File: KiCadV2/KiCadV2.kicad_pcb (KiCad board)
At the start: 2 copper layers, 76.4 x 51.6 mm, 141 parts, among them J1 USB_C_Receptacle_PowerOnly_6P, J3 Screw_Terminal_01x02, J4 Screw_Terminal_01x02, U1 MT3608, U10 NC7SZ157P6X, U11 NC7SZ157P6X, U12 NC7SZ157P6X, U13 NC7SZ157P6X, U14 74LV08AT14-13, U15 HIP4080A, U16 NC7SZ157P6X, U17 MX3502S, U18 MX3502S, U2 74HC595, U22 DMHT10H032LFJ, U26 MX3502S, U3 NC7SZ157P6X, U30 DMHT10H032LFJ, U31 INA240A1D, U32 NC7SZ157P6X, U33 NC7SZ157P6X, U34 NC7SZ157P6X, U35 NC7SZ157P6X, U36 NC7SZ157P6X, U37 NC7SZ157P6X, U38 74LV08AT14-13, U39 HIP4080A, U4 NC7SZ157P6X, U40 MCP6002-xSN, U41 CJ432, U5 MX3502S, U6 NC7SZ157P6X, U7 DAC082S085CISDX/NOPB, U8 NC7SZ157P6X, U9 NC7SZ157P6X

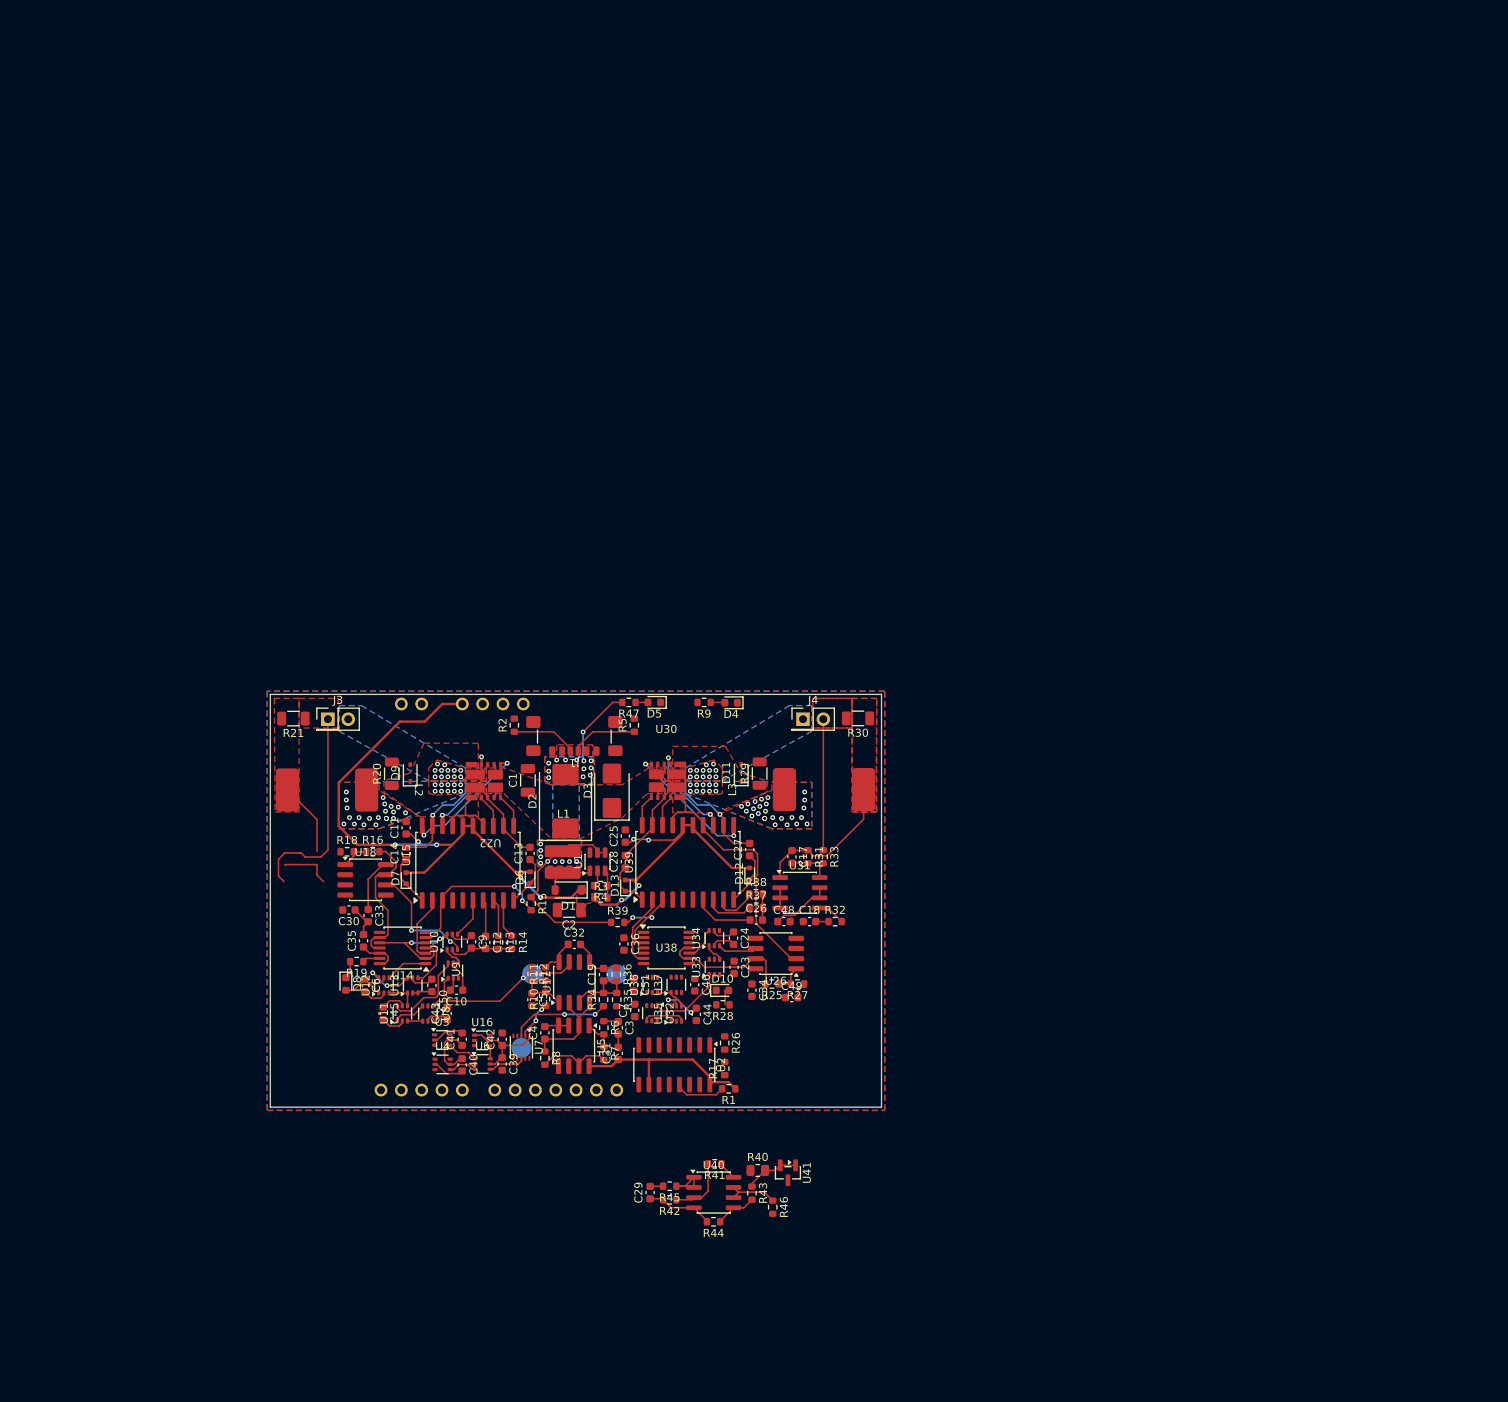
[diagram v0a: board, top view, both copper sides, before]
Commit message: DAC logic
- Internal connections done
- Spacing, shorts, nets, etc verified
- Grouped
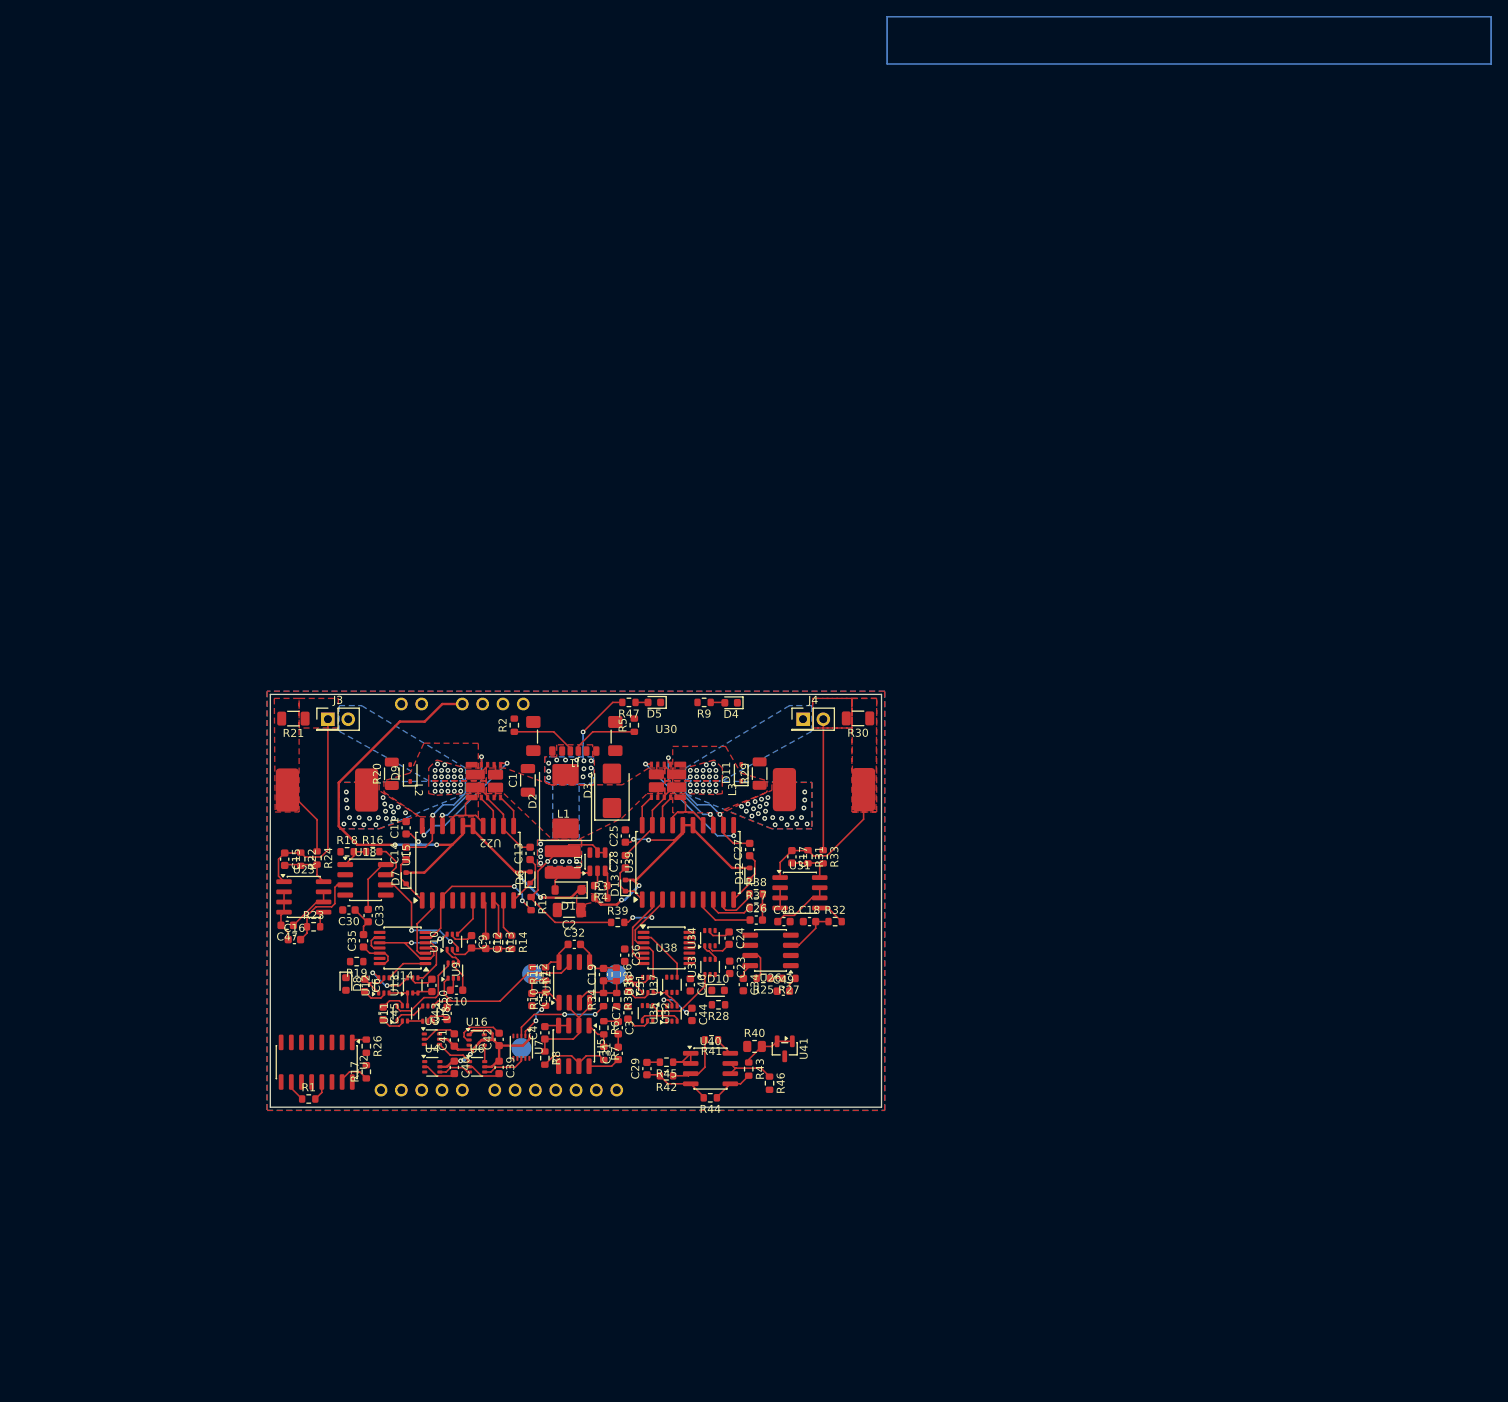
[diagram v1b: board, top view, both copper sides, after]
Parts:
- added C15: 100n, Capacitor_SMD:C_0603_1608Metric, F.Cu at (59.6, 143.2)
- added C16: 100n, Capacitor_SMD:C_0603_1608Metric, F.Cu at (60.8, 153.2)
- added C47: 100n, Capacitor_SMD:C_0603_1608Metric, F.Cu at (59.9, 151.5)
- added R22: 820, Resistor_SMD:R_0603_1608Metric, F.Cu at (61.6, 143.2)
- added R23: 1k, Resistor_SMD:R_0603_1608Metric, F.Cu at (63.2, 151.6)
- added R24: 1k, Resistor_SMD:R_0603_1608Metric, F.Cu at (63.6, 143.0)
- added U23: INA240A1D, Package_SO:SOIC-8_3.9x4.9mm_P1.27mm, F.Cu at (62.0, 147.9)
- moved R1 52.5 mm to (62.6, 173.2), turned to 0 degrees
- moved R17 44.8 mm to (69.8, 169.8)
- moved R26 44.8 mm to (69.8, 166.6)
- moved U2 44.7 mm to (63.6, 168.6)
- moved C29 15.5 mm to (104.9, 169.4)
- moved R40 15.5 mm to (118.3, 166.6)
- moved R41 15.5 mm to (113.0, 165.8)
- moved R42 15.5 mm to (107.3, 170.3)
- moved R43 15.5 mm to (117.6, 169.4)
- moved R44 15.5 mm to (112.8, 173.0)
- moved R45 15.5 mm to (107.3, 168.6)
- moved R46 15.5 mm to (120.2, 171.2)
- moved U40 15.5 mm to (112.8, 169.4)
- moved U41 15.5 mm to (122.1, 166.9)
- moved C36 1.40 mm to (102.1, 155.2)
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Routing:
- net /PerCoil1/OC_SENSE: track 32.3 -> 7.73 mm
- net GND: track 61.3 -> 81.1 mm
- net /PerCoil1/~{OC1}: track 16.7 -> 4.17 mm
- net /Analog1: track 0.00 -> 10.9 mm
- net /PerCoil/~{OC1}: track 18.4 -> 7.61 mm
- net Net-(U37-Z): track 0.00 -> 7.25 mm
- net /PerCoil1/SignalProcessingChain/Current_Dir: track 4.92 -> 0.00 mm
- net /Analog2: track 1.60 -> 6.43 mm
- net Net-(U36-Z): track 0.00 -> 4.61 mm
- net Net-(D8-K): track 4.43 -> 0.00 mm
- net /PerCoil1/SignalProcessingChain/EN: track 4.23 -> 0.00 mm
- net /D1: track 6.38 -> 2.46 mm
- net /EN1: track 0.00 -> 3.75 mm
- net Net-(U26A-+): track 3.82 -> 1.52 mm
- net Net-(R23-Pad2): track 0.00 -> 2.00 mm
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
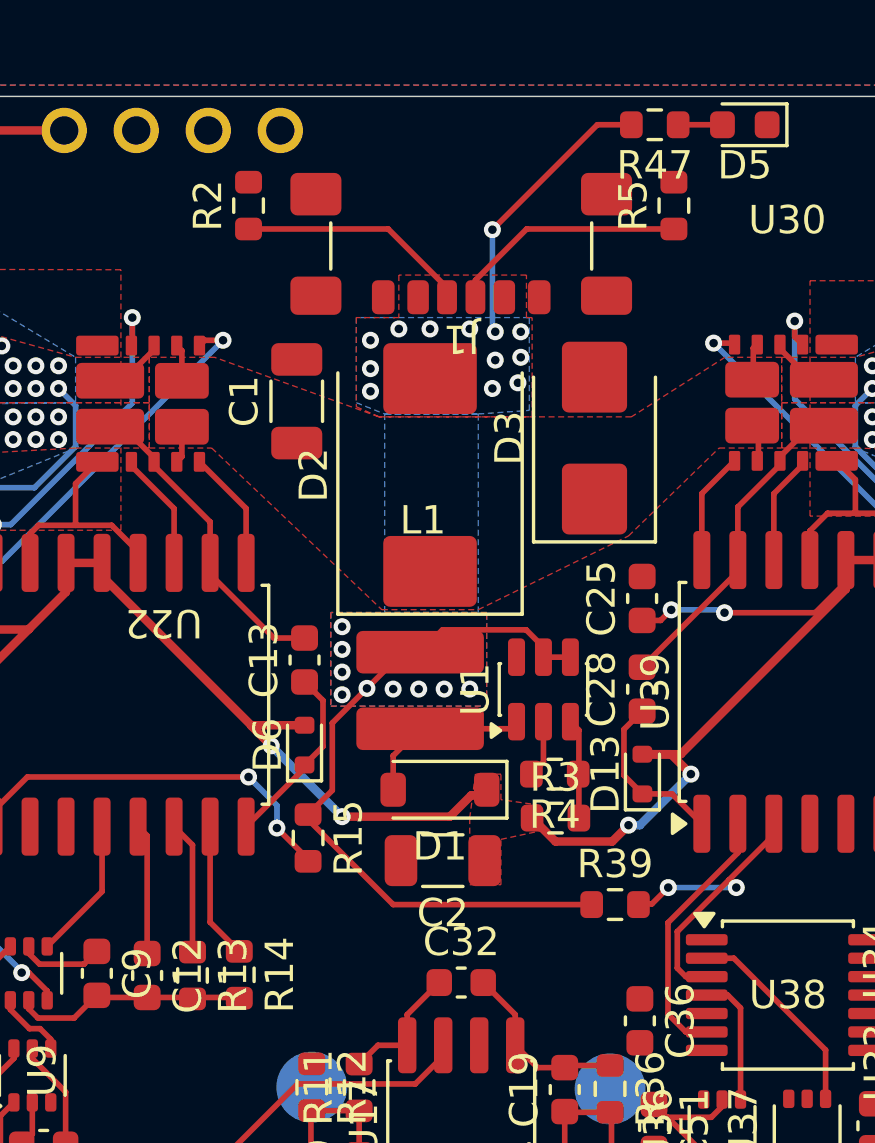
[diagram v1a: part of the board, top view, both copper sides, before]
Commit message: USBC power & Boost SMPS done
- Internal connections done
- Spacing, shorts, nets, etc verified
- Grouped
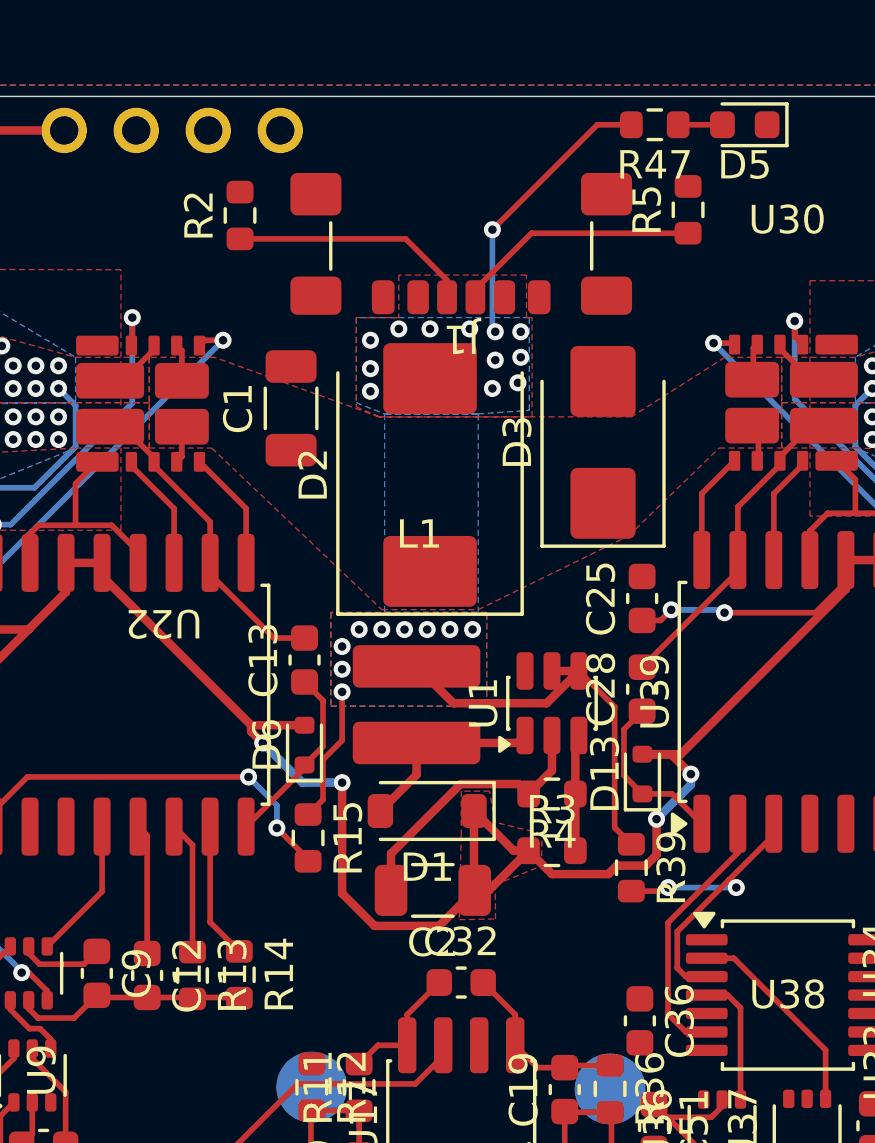
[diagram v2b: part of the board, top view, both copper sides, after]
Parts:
- moved R39 1.42 mm to (101.8, 149.8), turned to -90 degrees
- moved R3 1.16 mm to (99.0, 149.2)
- moved C2 1.11 mm to (94.8, 150.6)
- moved D1 0.87 mm to (94.6, 147.8)
- moved R4 0.71 mm to (99.0, 147.2)
- moved U1 0.57 mm to (99.0, 144.0)
- moved R5 0.52 mm to (103.8, 126.6)
- moved L1 0.52 mm to (94.2, 136.7)
- moved R2 0.46 mm to (88.0, 126.8)
- moved D3 0.34 mm to (100.8, 134.8)
- moved C1 0.32 mm to (89.8, 133.6)
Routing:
- net +12V: track 110.8 -> 124.2 mm
- net GND: track 81.1 -> 88.8 mm
- net VBUS: track 34.3 -> 29.5 mm
- net Net-(D1-A): track 6.05 -> 6.86 mm
- net Net-(J1-CC2): track 7.86 -> 8.50 mm
- net Net-(U1-FB): track 3.52 -> 4.11 mm

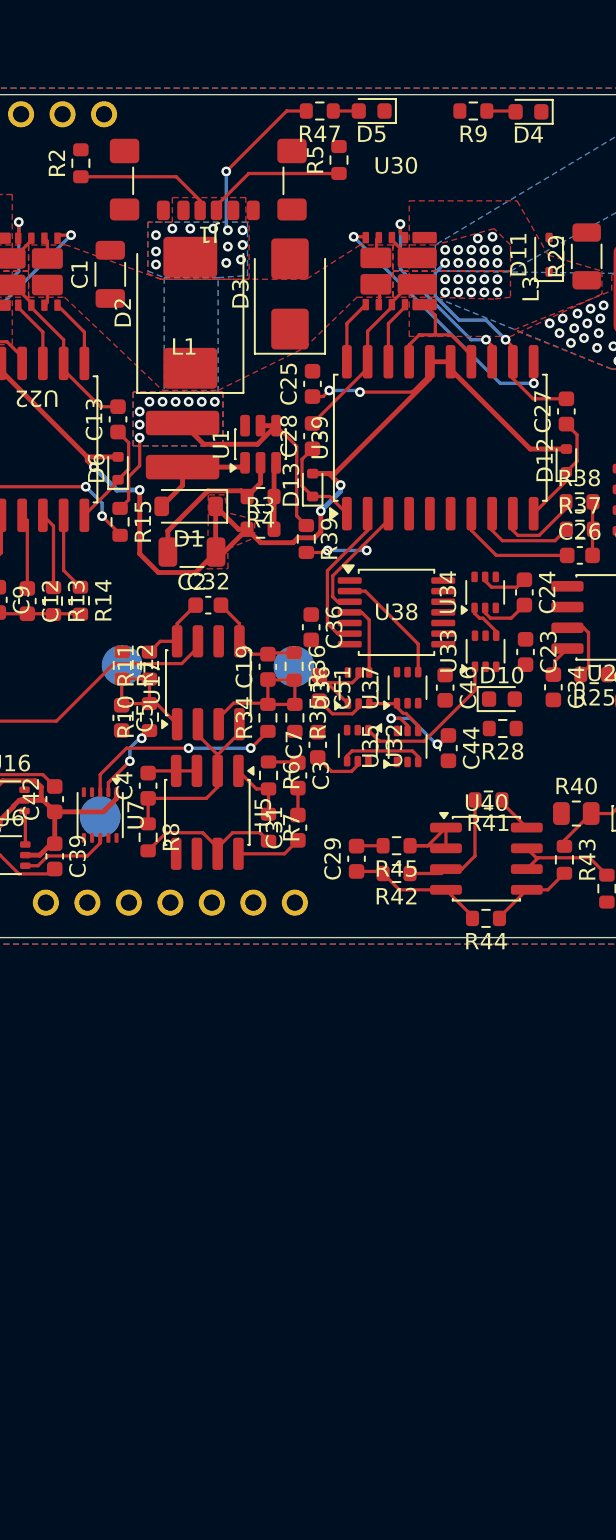
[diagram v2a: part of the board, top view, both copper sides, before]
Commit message: Triangle wave done
- Internal connections done
- Spacing, shorts, nets, etc verified
- Grouped
*Doesn't fit now...
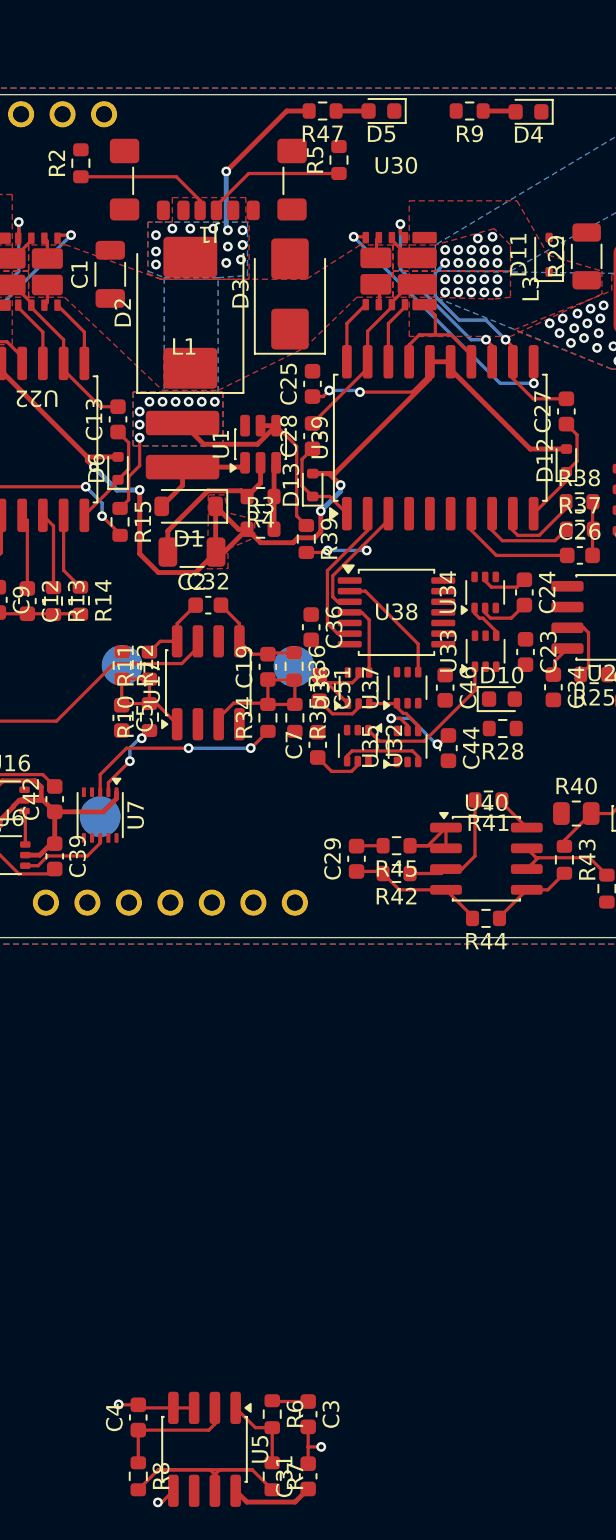
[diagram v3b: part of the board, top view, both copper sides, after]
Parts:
- moved C31 39.7 mm to (101.9, 207.2)
- moved R7 39.7 mm to (99.7, 207.2)
- moved R8 39.1 mm to (91.5, 207.2)
- moved C3 39.1 mm to (101.9, 203.4)
- moved R6 39.1 mm to (99.7, 203.4)
- moved U5 39.0 mm to (95.6, 205.5)
- moved C4 38.7 mm to (91.5, 203.6)
- moved D5 0.60 mm to (106.4, 123.6)
- moved R9 0.23 mm to (111.8, 123.6)
- moved R47 0.17 mm to (102.8, 123.6)
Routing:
- net /Vsq: track 8.80 -> 16.2 mm
- net GND: track 88.8 -> 93.3 mm, vias 0 -> 3
- net /Vtri: track 11.7 -> 7.83 mm
- net +5V: track 103.9 -> 104.9 mm
- net Net-(U5A-+): track 3.85 -> 4.89 mm
